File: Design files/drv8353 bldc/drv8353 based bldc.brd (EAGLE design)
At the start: 127 x 127 mm, 112 parts, among them IC1 DRV8353RSRGZT, J3 2X6 FEMALE, J4 B06B-HCMKK

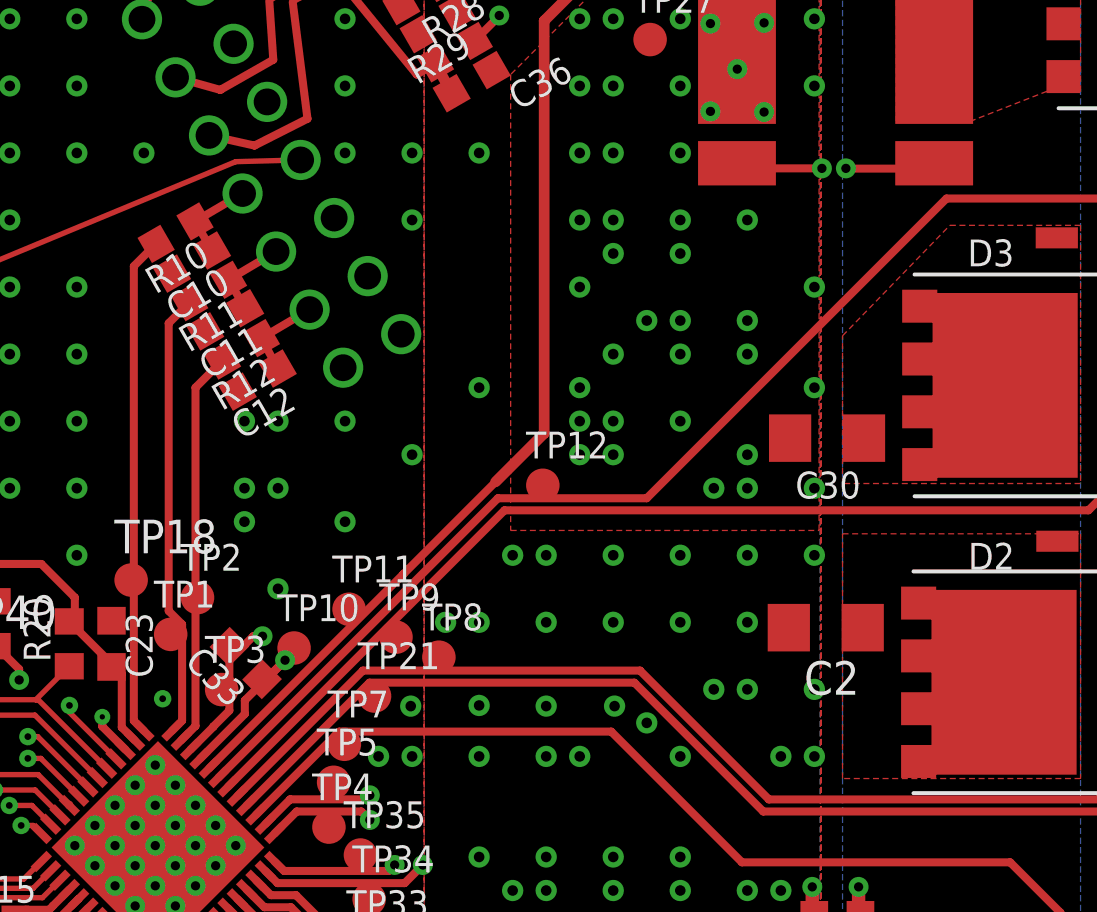
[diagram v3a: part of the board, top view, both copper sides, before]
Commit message: moved CPHASE current sense capacitor to be consistent with other phases
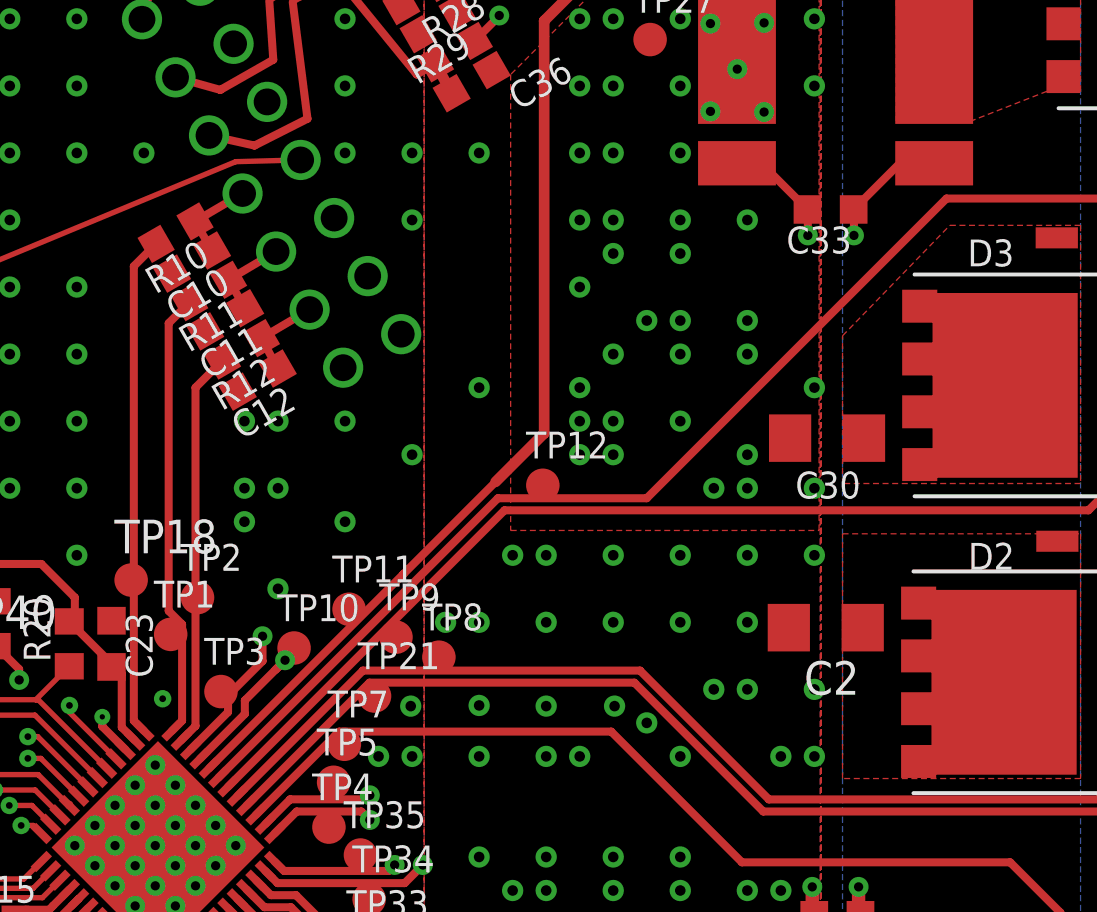
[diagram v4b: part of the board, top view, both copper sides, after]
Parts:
- moved C33 28.0 mm to (79.4, 105.8), turned to 180 degrees
- moved TP3 0.08 mm to (56.3, 87.5)
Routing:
- net GND: vias 1186 -> 1185
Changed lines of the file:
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@@
 <attribute name="SPICEPREFIX" value="C" x="-5.479196875" y="197.183196875" size="1.778" layer="27" rot="R180" display="off"/>
 </element>
-<element name="C33" library="rcl" library_urn="urn:adsk.eagle:library:334" package="C0603K" package3d_urn="urn:adsk.eagle:package:23680/2" value="1000 pF" x="57.1978" y="88.6278" smashed="yes" rot="R135">
-<attribute name="NAME" x="57.303865625" y="87.60249375" size="1.016" layer="25" rot="R135"/>
-<attribute name="POPULARITY" value="30" x="75.1583125" y="237.700046875" size="1.778" layer="27" rot="R135" display="off"/>
-<attribute name="SPICEPREFIX" value="C" x="75.1583125" y="237.700046875" size="1.778" layer="27" rot="R135" display="off"/>
+<element name="C33" library="rcl" library_urn="urn:adsk.eagle:library:334" package="C0603K" package3d_urn="urn:adsk.eagle:package:23680/2" value="1000 pF" x="79.3526" y="105.8092" smashed="yes" rot="R180">
+<attribute name="NAME" x="80.152603125" y="105.1592" size="1.016" layer="25" rot="R180"/>
+<attribute name="POPULARITY" value="30" x="-13.35739375" y="223.91919375" size="1.778" layer="27" rot="R180" display="off"/>
+<attribute name="SPICEPREFIX" value="C" x="-13.35739375" y="223.91919375" size="1.778" layer="27" rot="R180" display="off"/>
 </element>
 <element name="C34" library="rcl" library_urn="urn:adsk.eagle:library:334" package="C0603K" package3d_urn="urn:adsk.eagle:package:23680/2" value=".047uF" x="61.9222" y="117.2536" smashed="yes" rot="R30">
@@
 <attribute name="VALUE" x="70.052" y="73.1014" size="1.016" layer="27"/>
 </element>
-<element name="TP3" library="testpad" library_urn="urn:adsk.eagle:library:385" package="B1,27" package3d_urn="urn:adsk.eagle:package:27944/2" value="TPB1,27" x="56.2864" y="87.6224" smashed="yes">
-<attribute name="NAME" x="55.6514" y="88.6384" size="1.016" layer="25" ratio="10"/>
-<attribute name="POPULARITY" value="19" x="152.8064" y="-45.7276" size="1.778" layer="27" display="off"/>
-<attribute name="TP_SIGNAL_NAME" value="" x="55.6514" y="85.7174" size="1" layer="37"/>
-<attribute name="VALUE" x="55.6502" y="88.3856" size="1.016" layer="27"/>
+<element name="TP3" library="testpad" library_urn="urn:adsk.eagle:library:385" package="B1,27" package3d_urn="urn:adsk.eagle:package:27944/2" value="TPB1,27" x="56.261" y="87.5462" smashed="yes">
+<attribute name="NAME" x="55.626" y="88.5622" size="1.016" layer="25" ratio="10"/>
+<attribute name="POPULARITY" value="19" x="152.781" y="-45.8038" size="1.778" layer="27" display="off"/>
+<attribute name="TP_SIGNAL_NAME" value="" x="55.626" y="85.6412" size="1" layer="37"/>
+<attribute name="VALUE" x="55.6248" y="88.3094" size="1.016" layer="27"/>
 </element>
 <element name="TP32" library="testpad" library_urn="urn:adsk.eagle:library:385" package="B1,27" package3d_urn="urn:adsk.eagle:package:27944/2" value="TPB1,27" x="96.9264" y="53.8064" smashed="yes">
@@
 <wire x1="58.6880125" y1="88.7335875" x2="58.676896875" y2="88.744703125" width="0.3048" layer="15"/>
 <wire x1="58.676896875" y1="89.303503125" x2="58.676896875" y2="88.744703125" width="0.3048" layer="15"/>
-<wire x1="58.676896875" y1="89.303503125" x2="71.91319375" y2="102.5398" width="0.3048" layer="15"/>
-<wire x1="79.9338" y1="107.3658" x2="79.943" y2="107.3566" width="0.3048" layer="1"/>
+<wire x1="71.68459375" y1="102.3112" x2="58.676896875" y2="89.303503125" width="0.3048" layer="15"/>
+<wire x1="80.2386" y1="104.8258" x2="80.2478" y2="104.8166" width="0.3048" layer="1"/>
 <wire x1="83.2778" y1="107.5598" x2="83.0746" y2="107.3566" width="0.3048" layer="1"/>
-<wire x1="83.0746" y1="107.3566" x2="79.943" y2="107.3566" width="0.3048" layer="1"/>
-<via x="79.9338" y="107.3658" extent="1-16" drill="0.35"/>
-<wire x1="79.9338" y1="107.3658" x2="79.6544" y2="107.0864" width="0.3048" layer="15"/>
-<wire x1="79.6544" y1="107.0864" x2="79.6544" y2="105.791" width="0.3048" layer="15"/>
-<wire x1="79.6544" y1="105.791" x2="76.4032" y2="102.5398" width="0.3048" layer="15"/>
-<wire x1="76.4032" y1="102.5398" x2="71.91319375" y2="102.5398" width="0.3048" layer="15"/>
-<wire x1="57.816515625" y1="88.00908125" x2="57.96350625" y2="88.00908125" width="0.3048" layer="1"/>
-<wire x1="58.6880125" y1="88.7335875" x2="57.96350625" y2="88.00908125" width="0.3048" layer="1"/>
-<wire x1="83.2778" y1="107.5598" x2="82.9818" y2="107.1118" width="0" layer="19" extent="1-1"/>
+<via x="80.2386" y="104.8258" extent="1-16" drill="0.35"/>
+<wire x1="58.6880125" y1="88.7335875" x2="58.31910625" y2="88.36468125" width="0.3048" layer="1"/>
+<wire x1="80.2386" y1="104.8258" x2="79.6036" y2="104.1908" width="0.3048" layer="15"/>
+<wire x1="79.6036" y1="104.1908" x2="79.6036" y2="103.31561875" width="0.3048" layer="15"/>
+<wire x1="79.6036" y1="103.31561875" x2="78.59918125" y2="102.3112" width="0.3048" layer="15"/>
+<wire x1="78.59918125" y1="102.3112" x2="71.68459375" y2="102.3112" width="0.3048" layer="15"/>
+<wire x1="80.2276" y1="105.8092" x2="81.9782" y2="107.5598" width="0.3048" layer="1"/>
+<wire x1="81.9782" y1="107.5598" x2="83.2778" y2="107.5598" width="0.3048" layer="1"/>
+<wire x1="80.2276" y1="105.8092" x2="80.2386" y2="105.7982" width="0.3048" layer="1"/>
+<wire x1="80.2386" y1="105.7982" x2="80.2386" y2="104.8258" width="0.3048" layer="1"/>
+<wire x1="83.0746" y1="107.3566" x2="82.9818" y2="107.1118" width="0" layer="19" extent="1-1"/>
 <wire x1="59.0296" y1="89.196" x2="58.6880125" y2="88.7335875" width="0" layer="19" extent="1-1"/>
 </signal>
@@
 <via x="71.12" y="97.79" extent="1-16" drill="0.4"/>
 <via x="71.12" y="100.33" extent="1-16" drill="0.4"/>
-<via x="78.74" y="102.87" extent="1-16" drill="0.4"/>
 <via x="71.12" y="105.41" extent="1-16" drill="0.4"/>
 <via x="73.66" y="105.41" extent="1-16" drill="0.4"/>
@@
 <contactref element="U$5" pad="E2"/>
 <via x="57.8358" y="89.6423875" extent="1-16" drill="0.35"/>
-<wire x1="55.9730125" y1="86.2128875" x2="55.111234375" y2="85.351109375" width="0.3048" layer="1"/>
-<wire x1="55.9730125" y1="86.2128875" x2="55.9730125" y2="86.2225" width="0.3048" layer="1"/>
 <wire x1="57.8358" y1="89.6423875" x2="58.3438" y2="89.6423875" width="0.3048" layer="15"/>
-<wire x1="71.6984125" y1="102.997" x2="58.3438" y2="89.6423875" width="0.3048" layer="15"/>
-<via x="79.025" y="107.3658" extent="1-16" drill="0.35"/>
-<wire x1="79.1774" y1="105.9942" x2="76.1802" y2="102.997" width="0.3048" layer="15"/>
-<wire x1="79.1774" y1="107.2134" x2="79.1774" y2="105.9942" width="0.3048" layer="15"/>
-<wire x1="79.1774" y1="107.2134" x2="79.025" y2="107.3658" width="0.3048" layer="15"/>
-<wire x1="71.6984125" y1="102.997" x2="76.1802" y2="102.997" width="0.3048" layer="15"/>
-<wire x1="79.025" y1="107.3658" x2="76.0018" y2="107.3658" width="0.3048" layer="1"/>
+<wire x1="71.4698125" y1="102.7684" x2="58.3438" y2="89.6423875" width="0.3048" layer="15"/>
+<via x="78.4916" y="104.8258" extent="1-16" drill="0.35"/>
 <wire x1="76.0018" y1="107.3658" x2="75.8078" y2="107.5598" width="0.3048" layer="1"/>
-<wire x1="57.482953125" y1="89.6423875" x2="57.08708125" y2="89.246515625" width="0.3048" layer="1"/>
-<wire x1="56.57908125" y1="89.246515625" x2="57.08708125" y2="89.246515625" width="0.3048" layer="1"/>
-<wire x1="57.8358" y1="89.6423875" x2="57.482953125" y2="89.6423875" width="0.3048" layer="1"/>
-<wire x1="56.57908125" y1="89.246515625" x2="56.57908125" y2="86.82856875" width="0.3048" layer="1"/>
-<wire x1="56.57908125" y1="86.82856875" x2="55.9730125" y2="86.2225" width="0.3048" layer="1"/>
-<wire x1="56.57908125" y1="89.246515625" x2="56.2864" y2="87.6224" width="0" layer="19" extent="1-1"/>
+<wire x1="57.8358" y1="89.6423875" x2="57.8358" y2="88.699834375" width="0.3048" layer="1"/>
+<wire x1="56.52828125" y1="87.392315625" x2="57.8358" y2="88.699834375" width="0.3048" layer="1"/>
+<wire x1="56.52828125" y1="86.76815625" x2="56.52828125" y2="87.392315625" width="0.3048" layer="1"/>
+<wire x1="55.111234375" y1="85.351109375" x2="56.52828125" y2="86.76815625" width="0.3048" layer="1"/>
+<wire x1="78.4916" y1="104.8258" x2="79.1464" y2="104.171" width="0.3048" layer="15"/>
+<wire x1="79.1464" y1="104.171" x2="79.1464" y2="103.5304" width="0.3048" layer="15"/>
+<wire x1="79.1464" y1="103.5304" x2="78.3844" y2="102.7684" width="0.3048" layer="15"/>
+<wire x1="78.3844" y1="102.7684" x2="71.4698125" y2="102.7684" width="0.3048" layer="15"/>
+<wire x1="75.8078" y1="107.5598" x2="76.727" y2="107.5598" width="0.3048" layer="1"/>
+<wire x1="76.727" y1="107.5598" x2="78.4776" y2="105.8092" width="0.3048" layer="1"/>
+<wire x1="78.4776" y1="105.8092" x2="78.4916" y2="105.7952" width="0.3048" layer="1"/>
+<wire x1="78.4916" y1="105.7952" x2="78.4916" y2="104.8258" width="0.3048" layer="1"/>
+<wire x1="55.111234375" y1="85.351109375" x2="56.261" y2="87.5462" width="0" layer="19" extent="1-1"/>
 </signal>
 <signal name="GLC">

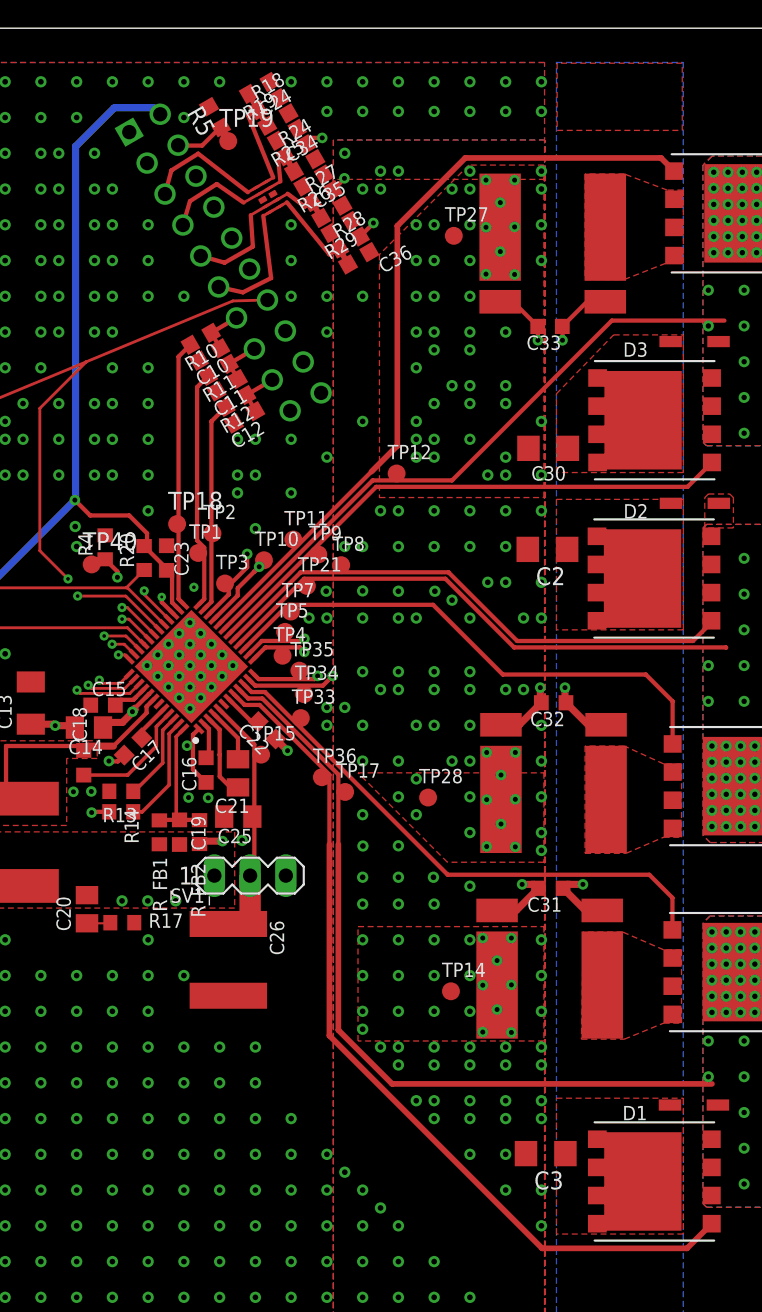
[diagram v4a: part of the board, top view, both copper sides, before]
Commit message: added little bits of routing to resolve all air wires
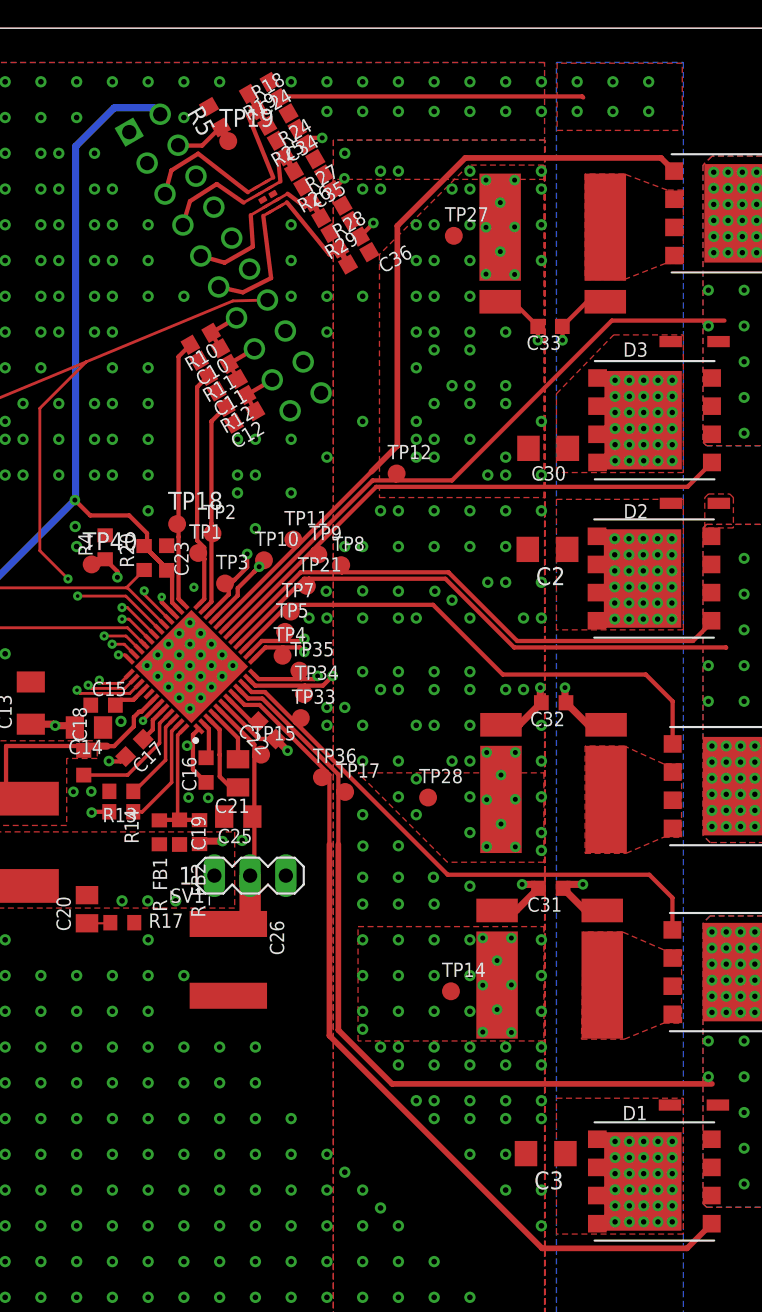
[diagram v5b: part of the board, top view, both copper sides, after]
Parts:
- moved C17 0.14 mm to (49.8, 75.9)
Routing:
- net VDRAIN: track 53.1 -> 81.2 mm, vias 3 -> 100
- net GND: track 12.4 -> 7.95 mm
- net 3V3: track 99.5 -> 101.9 mm
- net SNC: track 38.7 -> 39.5 mm
- net SPB: track 30.0 -> 30.7 mm
- net DRV_VM: track 16.5 -> 17.1 mm
- net SNA: track 32.9 -> 33.5 mm
- net SPA: track 37.9 -> 38.5 mm
- net SOB: track 16.9 -> 17.5 mm
- net SPC: track 40.5 -> 41.1 mm
- net SNB: track 27.4 -> 28.0 mm
- net BPHASE: track 129.1 -> 129.7 mm
- net GLC: track 56.1 -> 56.7 mm
- net VCC: track 2.71 -> 3.24 mm
- net GHB: track 38.6 -> 39.1 mm
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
